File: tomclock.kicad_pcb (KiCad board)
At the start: 4 copper layers, 200 x 200 mm, 163 parts, among them J1 USB_BOOT, J2 USB_C_Receptacle_USB2.0, J3 RESET, J4 Conn_02x10_Odd_Even, U1 W25Q128JVS, U2 XC6206P332MR, U3 RP2040, U4 74HCT245, Y1 12MHz

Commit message: PCB: Updated new components, removed old paths
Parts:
- removed J3: RESET, Connector_PinHeader_2.54mm:PinHeader_1x02_P2.54mm_Vertical
- removed J4: Conn_02x10_Odd_Even, Connector_IDC:IDC-Header_2x10_P2.54mm_Vertical
- added D1: SMF05CT1G, esd:SOT-363_L2.0-W1.3-P0.65-LS2.1-BR, F.Cu at (44.1, 200.8)
- added J5: Boot/Reset, Connector_PinHeader_2.54mm:PinHeader_2x02_P2.54mm_Vertical, F.Cu at (56.1, 148.3)
- J1: value USB_BOOT -> I2C_Conn; footprint Connector_PinHeader_2.54mm:PinHeader_1x02_P2.54mm_Vertical -> Connector_PinHeader_2.54mm:PinHeader_1x05_P2.54mm_Vertical
- moved J1 77.0 mm to (136.2, 151.8)
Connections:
- net /Circle_5 renamed /LEDCircle/SECOND_IN
- net /Digit_5 renamed /Digit1/DIGIT_IN
- J1 pad 2: Net-(J1-Pad2) -> +3V3
- R1 pad 1: Net-(J1-Pad2) -> /rp2040_base/USB_BOOT
- U3 pad 26: Net-(J3-Pad2) -> /rp2040_base/RESET
- U3 pad 28: /GPIO17 -> /rp2040_base/GPIO17
- U3 pad 29: /GPIO18 -> /GPIO19_I2C1_SCL
- U3 pad 30: /GPIO19 -> /GPIO19_I2C1_SDA
- U3 pad 31: /GPIO20 -> /rp2040_base/GPIO20
- U3 pad 32: /GPIO21 -> /rp2040_base/GPIO21
- U3 pad 34: /GPIO22 -> /rp2040_base/GPIO22
- U4 pad 11: /GPIO7_5 -> unconnected-(U4-B7-Pad11)
- U4 pad 12: /GPIO6_5 -> unconnected-(U4-B6-Pad12)
- U4 pad 13: /GPIO5_5 -> unconnected-(U4-B5-Pad13)
- U4 pad 14: /GPIO4_5 -> unconnected-(U4-B4-Pad14)
- U4 pad 15: /GPIO3_5 -> unconnected-(U4-B3-Pad15)
- U4 pad 16: /GPIO2_5 -> unconnected-(U4-B2-Pad16)
- U4 pad 4: /rp2040_base/GPIO2 -> unconnected-(U4-A2-Pad4)
- U4 pad 5: /rp2040_base/GPIO3 -> unconnected-(U4-A3-Pad5)
- U4 pad 6: /rp2040_base/GPIO4 -> unconnected-(U4-A4-Pad6)
- U4 pad 7: /rp2040_base/GPIO5 -> unconnected-(U4-A5-Pad7)
- U4 pad 8: /rp2040_base/GPIO6 -> unconnected-(U4-A6-Pad8)
- U4 pad 9: /rp2040_base/GPIO7 -> unconnected-(U4-A7-Pad9)
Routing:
- net /GPIO20: track 105.0 -> 0.00 mm, vias 4 -> 0
- net /GPIO17: track 104.9 -> 0.00 mm, vias 4 -> 0
- net /GPIO19: track 104.3 -> 0.00 mm, vias 4 -> 0
- net /GPIO21: track 104.1 -> 0.00 mm, vias 4 -> 0
- net /GPIO18: track 103.7 -> 0.00 mm, vias 4 -> 0
- net /GPIO19_I2C1_SCL: track 0.00 -> 102.1 mm, vias 0 -> 3
- net /GPIO22: track 99.4 -> 0.00 mm, vias 4 -> 0
- net /GPIO19_I2C1_SDA: track 0.00 -> 97.1 mm, vias 0 -> 3
- net /rp2040_base/GPIO2: track 54.8 -> 0.00 mm, vias 2 -> 0
- net /rp2040_base/GPIO3: track 51.7 -> 0.00 mm, vias 2 -> 0
- net /rp2040_base/GPIO7: track 37.4 -> 0.00 mm, vias 2 -> 0
- net /rp2040_base/GPIO5: track 36.7 -> 0.00 mm, vias 4 -> 0
- net /GPIO7_5: track 36.6 -> 0.00 mm, vias 2 -> 0
- net /rp2040_base/GPIO4: track 36.6 -> 0.00 mm, vias 4 -> 0
- net /rp2040_base/GPIO6: track 35.0 -> 0.00 mm, vias 4 -> 0
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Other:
- board text removed: "3V3 Bank"
- board text removed: "5V Bank"
- board text removed: "Digit Cycle GPIO2 GPIO3 GPIO4 GPIO5 GPIO6 GPIO7 VBUS GND"
- board text removed: "GND GND GPIO17 GPIO18 GPI19 GPI20 GPI21 GPI22 3V3 GND"

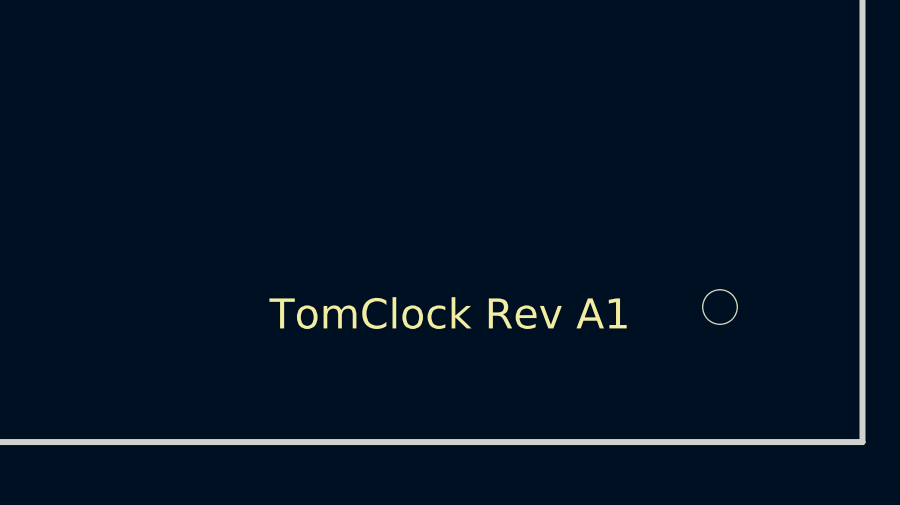
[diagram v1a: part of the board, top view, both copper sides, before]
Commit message: PCB: SilkScreen Updates
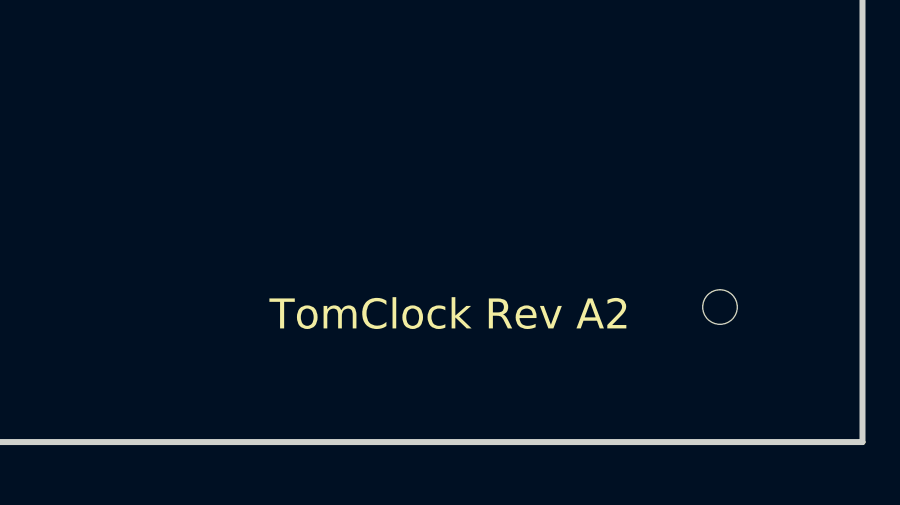
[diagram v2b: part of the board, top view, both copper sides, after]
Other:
- board text added: "GND VCC SDA SCL NC"
- board text added: "TomClock Rev A2"
- board text removed: "TomClock Rev A1"
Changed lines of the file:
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@@
   (gr_rect (start 20.75 13.5) (end 220.75 213.5)
     (stroke (width 0.2) (type solid)) (fill none) (layer "Edge.Cuts"))
+  (gr_text "GND\nVCC\nSDA\nSCL\nNC" (at 134.35 163.1) (layer "B.SilkS")
+    (effects (font (size 1.6 1.6) (thickness 0.15)) (justify left bottom mirror))
+  )
   (gr_text "JLCJLCJLCJLC" (at 102.5 158) (layer "F.SilkS")
     (effects (font (size 1 1) (thickness 0.15)))
   )
-  (gr_text "TomClock Rev A1" (at 207 209.25) (layer "F.SilkS")
+  (gr_text "TomClock Rev A2" (at 207 209.25) (layer "F.SilkS")
     (effects (font (size 1 1) (thickness 0.15)))
   )

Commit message: JLC: Fixup for JLC Production
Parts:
- DS51: value S2812B -> WS2812B
- R5: value 27.4 -> 27.6; footprint Resistor_SMD:R_0201_0603Metric -> Resistor_SMD:R_1206_3216Metric
- R6: footprint Resistor_SMD:R_0201_0603Metric -> Resistor_SMD:R_1206_3216Metric
- U4: footprint Package_SO:SOIC-20W_7.5x12.8mm_P1.27mm -> esd:SOIC-20_L13.3-W5.5-P1.27-LS7.8-BL
- moved R6 4.83 mm to (69.2, 171.4)
- moved R5 4.64 mm to (72.2, 171.3)
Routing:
- net Net-(U3-USB_DM): track 3.03 -> 7.59 mm
- net Net-(U3-USB_DP): track 3.02 -> 6.93 mm
- net /rp2040_base/USB_C_D-: track 59.5 -> 55.6 mm
- net /rp2040_base/USB_C_D+: track 59.3 -> 57.6 mm
- net /rp2040_base/GPIO0: track 58.2 -> 58.8 mm
- net /rp2040_base/GPIO1: track 57.3 -> 56.7 mm
